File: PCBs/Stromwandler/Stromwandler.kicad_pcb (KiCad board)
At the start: 2 copper layers, 30 x 30 mm, 10 parts, among them IC1 HO10-P_SP33, J1 Conn_02x05_Odd_Even, J4 2X

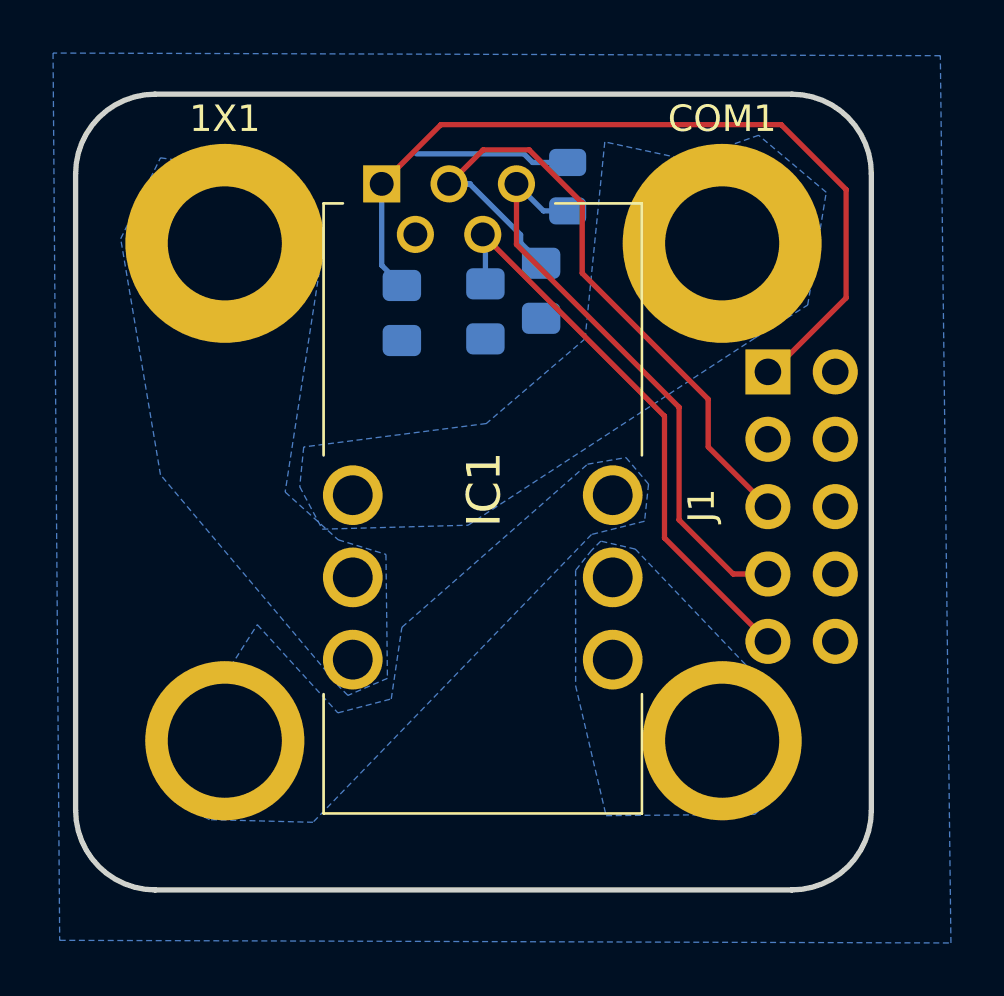
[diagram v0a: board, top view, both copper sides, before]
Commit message: Zusammenfuehrung
PCB und SCH Update zu 7-polig. Mehr übersichtlichkeit und Update Footprints Connectoren
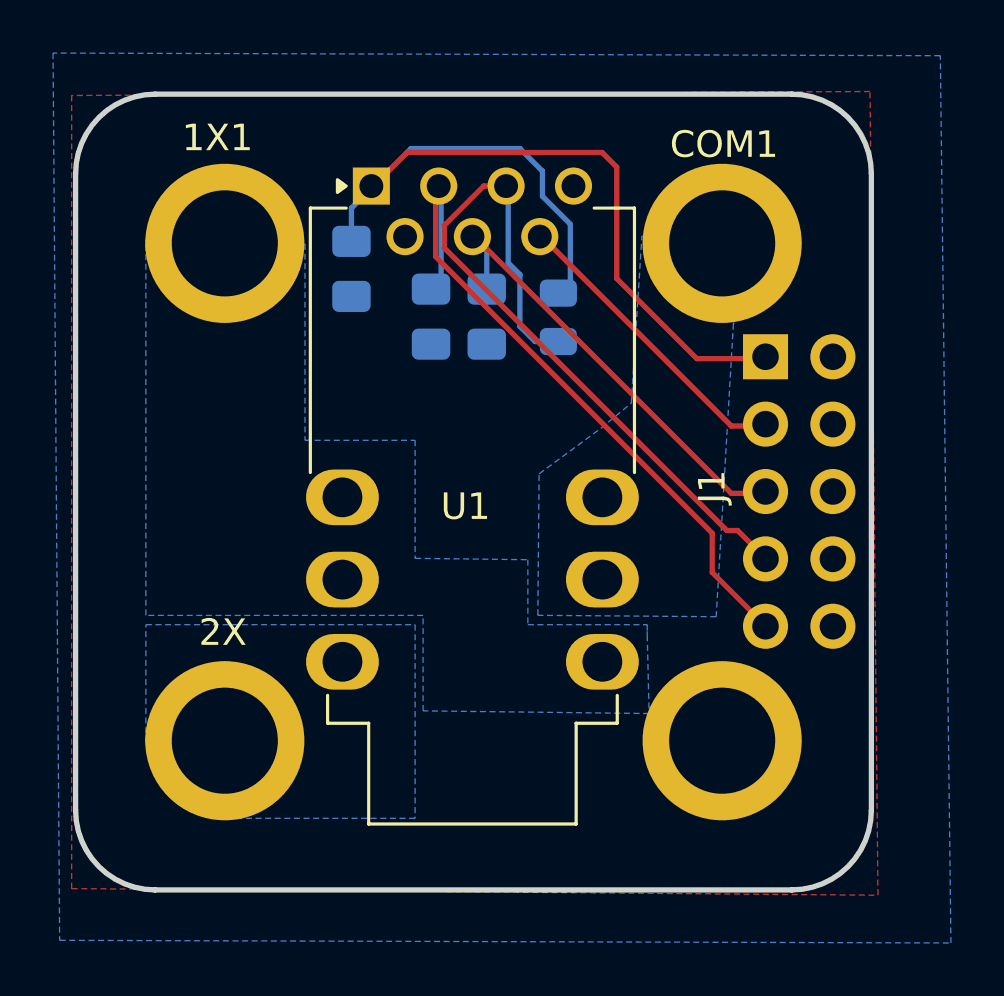
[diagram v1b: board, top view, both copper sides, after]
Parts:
- removed IC1: HO10-P_SP33, HO10_P_SP33:HO10PSP33
- added U1: HO15-NPxSP33, Sensor_Current:LEM_HO8-NP, F.Cu at (96.2, 88.5)
- moved R1 4.94 mm to (103.2, 93.4)
- moved C2 2.52 mm to (95.4, 91.6)
- moved C1 2.27 mm to (100.5, 93.4)
- moved C3 2.06 mm to (98.4, 93.4)
- moved J1 0.58 mm to (111.1, 94.8)
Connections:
- J1 pad 3: unconnected-(J1-Pin_3-Pad3) -> Net-(J1-Pin_3)
- J4 pad 1: Net-(IC1-RETENTION_PIN_4) -> unconnected-(J4-Pin_1-Pad1)
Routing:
- net Net-(J1-Pin_3): track 0.00 -> 11.5 mm
- net Net-(J1-Pin_5): track 26.4 -> 17.8 mm
- net Net-(J1-Pin_7): track 21.8 -> 28.1 mm
- net Net-(J1-Pin_9): track 21.7 -> 26.0 mm
- net Net-(J1-Pin_1): track 39.6 -> 36.0 mm
- net Net-(1X1-Pin_1): track 1.59 -> 0.00 mm
- net Net-(COM1-Pin_1): track 1.59 -> 0.00 mm
- net unconnected-(J4-Pin_1-Pad1): track 0.00 -> 1.07 mm
- net Net-(IC1-RETENTION_PIN_4): track 1.07 -> 0.00 mm
- added copper zone on F.Cu, net Net-(J1-Pin_10)
- removed copper zone on B.Cu, net Net-(IC1-RETENTION_PIN_4)
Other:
- board text added: "2X"
